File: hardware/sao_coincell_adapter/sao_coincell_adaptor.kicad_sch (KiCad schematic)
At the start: 1 part, among them J1 Conn_02x03_Odd_Even

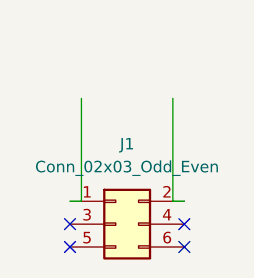
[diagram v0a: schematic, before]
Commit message: Restore SAO coin cell holder
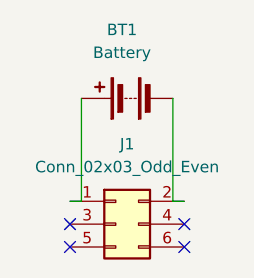
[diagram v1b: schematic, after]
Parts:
- added BT1: Battery, Battery:BatteryHolder_MYOUNG_BS-07-A1BJ001_CR2032, symbol Device:Battery
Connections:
- net at J1.1 (Pin_1): now also BT1.1 (+)
- net at J1.2 (Pin_2): now also BT1.2 (-)
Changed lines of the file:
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@@
+	)
+	(symbol
+		(lib_id "Device:Battery")
+		(at 109.22 62.23 90)
+		(unit 1)
+		(exclude_from_sim no)
+		(in_bom yes)
+		(on_board yes)
+		(dnp no)
+		(fields_autoplaced yes)
+		(property "Reference" "BT1"
+			(at 108.6485 54.61 90)
+			(effects
+				(font
+					(size 1.27 1.27)
+				)
+			)
+		)
+		(property "Value" "Battery"
+			(at 108.6485 57.15 90)
+			(effects
+				(font
+					(size 1.27 1.27)
+				)
+			)
+		)
+		(property "Footprint" "Battery:BatteryHolder_MYOUNG_BS-07-A1BJ001_CR2032"
+			(at 107.696 62.23 90)
+			(effects
+				(font
+					(size 1.27 1.27)
+				)
+				(hide yes)
+			)
+		)
+		(property "Datasheet" "~"
+			(at 107.696 62.23 90)
+			(effects
+				(font
+					(size 1.27 1.27)
+				)
+				(hide yes)
+			)
+		)
+		(property "Description" "Multiple-cell battery"
+			(at 109.22 62.23 0)
+			(effects
+				(font
+					(size 1.27 1.27)
+				)
+				(hide yes)
+			)
+		)
+		(pin "1"
+		)
+		(pin "2"
+		)
+		(instances
+			(project ""
+				(path "/3e7d9386-cd47-413a-8a37-d88668a03129"
+					(reference "BT1")
+					(unit 1)
+				)
+			)
+		)
 	)
 	(symbol

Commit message: Add hardware visual diff CI test
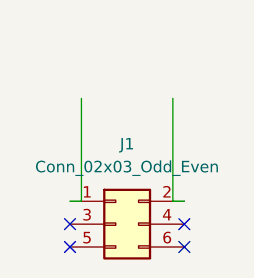
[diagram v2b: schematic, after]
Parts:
- removed BT1: Battery, Battery:BatteryHolder_MYOUNG_BS-07-A1BJ001_CR2032, symbol Device:Battery
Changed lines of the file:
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@@
-	)
-	(symbol
-		(lib_id "Device:Battery")
-		(at 109.22 62.23 90)
-		(unit 1)
-		(exclude_from_sim no)
-		(in_bom yes)
-		(on_board yes)
-		(dnp no)
-		(fields_autoplaced yes)
-		(property "Reference" "BT1"
-			(at 108.6485 54.61 90)
-			(effects
-				(font
-					(size 1.27 1.27)
-				)
-			)
-		)
-		(property "Value" "Battery"
-			(at 108.6485 57.15 90)
-			(effects
-				(font
-					(size 1.27 1.27)
-				)
-			)
-		)
-		(property "Footprint" "Battery:BatteryHolder_MYOUNG_BS-07-A1BJ001_CR2032"
-			(at 107.696 62.23 90)
-			(effects
-				(font
-					(size 1.27 1.27)
-				)
-				(hide yes)
-			)
-		)
-		(property "Datasheet" "~"
-			(at 107.696 62.23 90)
-			(effects
-				(font
-					(size 1.27 1.27)
-				)
-				(hide yes)
-			)
-		)
-		(property "Description" "Multiple-cell battery"
-			(at 109.22 62.23 0)
-			(effects
-				(font
-					(size 1.27 1.27)
-				)
-				(hide yes)
-			)
-		)
-		(pin "1"
-		)
-		(pin "2"
-		)
-		(instances
-			(project ""
-				(path "/3e7d9386-cd47-413a-8a37-d88668a03129"
-					(reference "BT1")
-					(unit 1)
-				)
-			)
-		)
 	)
 	(symbol
